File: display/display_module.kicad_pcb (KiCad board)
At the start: 2 copper layers, 38.5 x 20 mm, 14 parts, among them J1 DISPLAY FPC, J2 FPC LOGIC, J4 DF40

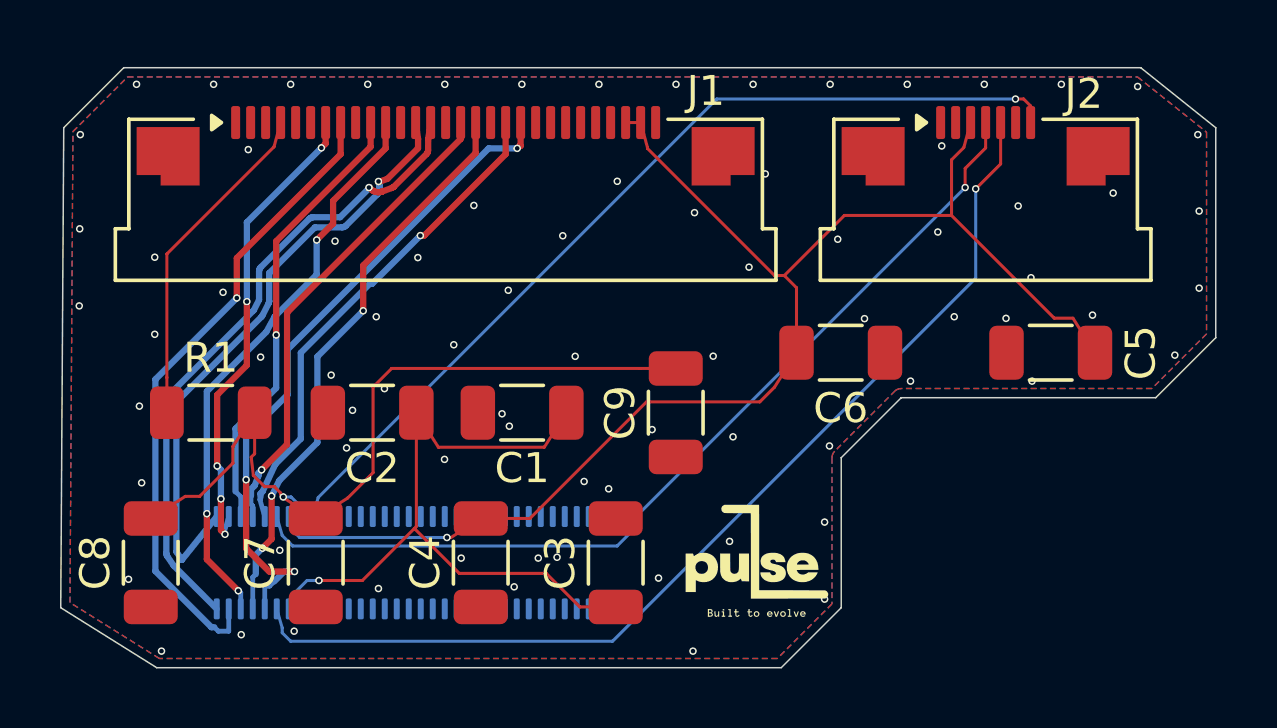
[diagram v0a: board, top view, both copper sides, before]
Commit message: fix the interrupted gnd plane by moving to 4 layers and adding gnd zones.
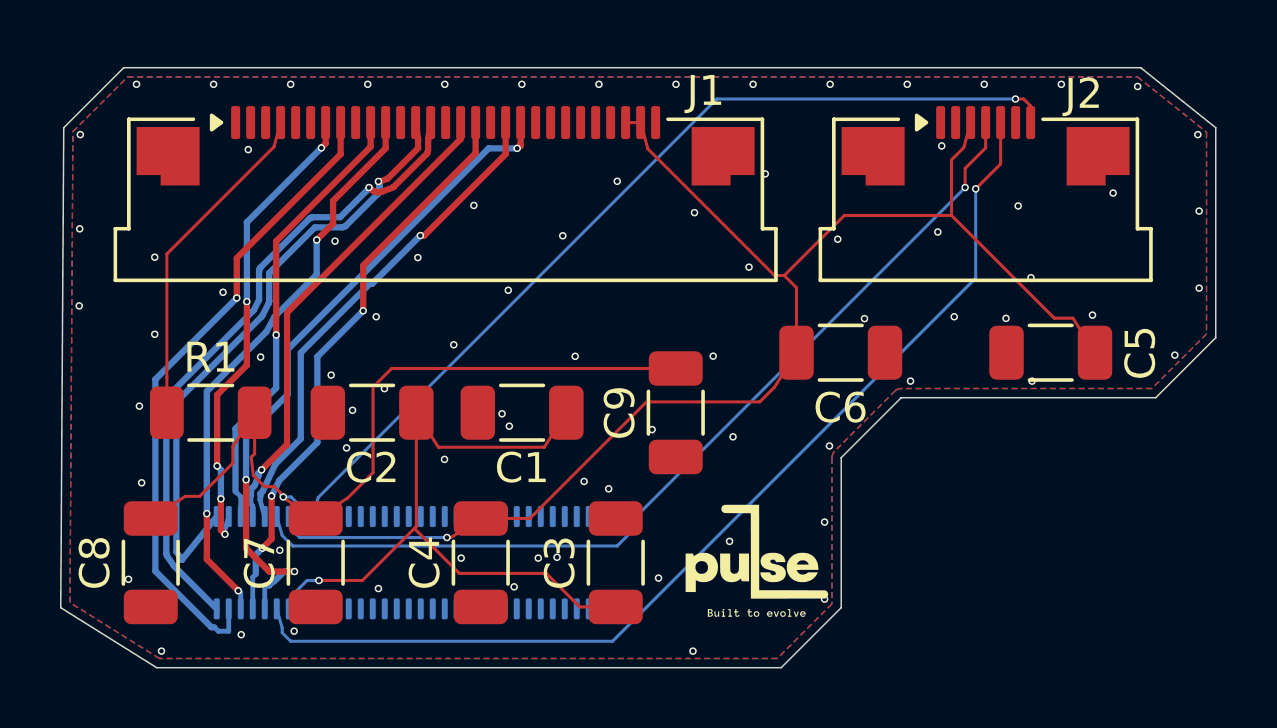
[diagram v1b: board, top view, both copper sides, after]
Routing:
- added copper zone on In1.Cu, net GND
- added copper zone on In2.Cu, net GND
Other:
- copper layers 2 -> 4

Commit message: concetrate center of mass ontop of display DF40c
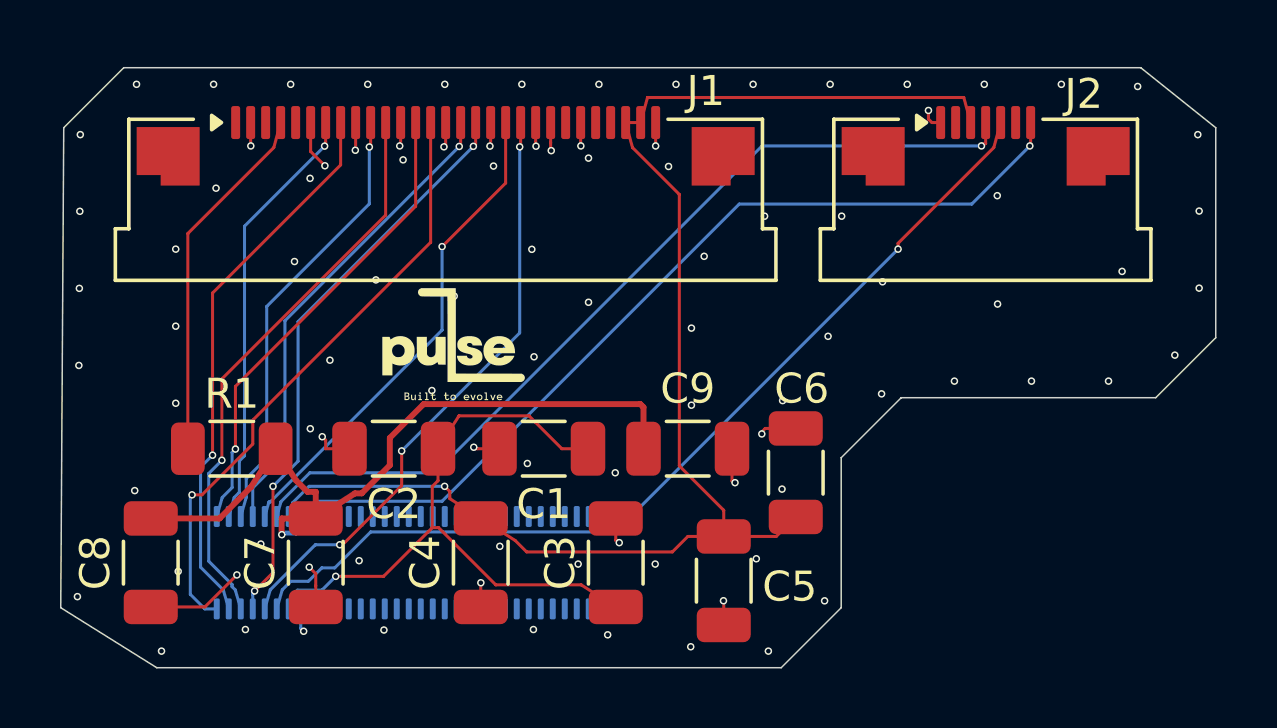
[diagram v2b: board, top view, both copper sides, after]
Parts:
- moved C5 13.3 mm to (139.6, 81.6), turned to 90 degrees
- moved G*** 12.4 mm to (130.6, 73.8)
- moved C6 4.27 mm to (142.0, 78.0), turned to -90 degrees
- moved C2 1.40 mm to (128.6, 77.2)
- moved C1 1.40 mm to (133.6, 77.2)
- moved R1 1.39 mm to (123.2, 77.2)
- moved C9 1.26 mm to (138.4, 77.2), turned to 180 degrees
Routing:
- net GND: track 0.00 -> 22.4 mm, vias 80 -> 96
- net DSI-CLK-N: track 20.5 -> 15.8 mm
- net DSI-0-P: track 21.5 -> 18.5 mm
- net I2C3-SDA: track 34.6 -> 31.8 mm
- net DSI-3-P: track 22.4 -> 20.2 mm
- net DSI-0-N: track 16.0 -> 14.4 mm, vias 5 -> 1
- net I2C3-SCL: track 31.2 -> 29.7 mm
- net +5V: track 23.4 -> 22.0 mm
- net +3.7VBAT: track 26.7 -> 25.4 mm
- net DSI-CLK-P: track 21.6 -> 20.3 mm
- net Net-(J1-Pin_4): track 11.2 -> 12.1 mm
- net RST: track 30.6 -> 30.0 mm
- net DSI-1-P: track 19.1 -> 19.0 mm, vias 3 -> 1
- removed copper zone on B.Cu, net GND
- removed copper zone on F.Cu, net GND

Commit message: final review change (board was ordered, prod ready verSion)
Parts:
- J1: value DISPLAY FPC -> THD THD0515-29CL-SN; footprint Connector_FFC-FPC:Amphenol_F32R-1A7x1-11029_1x29-1MP_P0.5mm_Horizontal -> Connector_FFC-FPC:FPC-29-P0.5
- J2: footprint Connector_FFC-FPC:Amphenol_F32Q-1A7x1-11007_1x07-1MP_P0.5mm_Horizontal -> Connector_FFC-FPC:FPC_7
- J4: footprint Connector_Hirose_DF40:Hirose_DF40C(2.0)-70DS-0.4V_2x35_P0.4mm -> Connector_Hirose_DF40:Hirose_DF40C-34DS-0.4V_2x17_P0.4mm
- moved J1 1.12 mm to (130.7, 70.3), turned to 180 degrees
- moved J2 1.10 mm to (148.2, 70.3), turned to 180 degrees
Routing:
- net Net-(J1-Pin_4): track 12.1 -> 21.7 mm
- net RST: track 30.0 -> 22.8 mm, vias 1 -> 3
- net DSI-3-N: track 16.4 -> 9.63 mm
- net I2C3-SDA: track 31.8 -> 25.9 mm
- net DSI-2-N: track 16.0 -> 10.5 mm
- net DSI-CLK-P: track 20.3 -> 15.0 mm
- net I2C3-SCL: track 29.7 -> 25.3 mm
- net GND: track 22.4 -> 18.3 mm, vias 96 -> 87
- net +3.3V: track 46.7 -> 42.7 mm, vias 1 -> 2
- net DSI-1-P: track 19.0 -> 16.5 mm
- net DSI-3-P: track 20.2 -> 18.2 mm, vias 3 -> 1
- net +3.7VBAT: track 25.4 -> 23.6 mm
- net DSI-0-N: track 14.4 -> 12.8 mm
- net DSI-2-P: track 19.3 -> 17.8 mm, vias 3 -> 1
- net DSI-CLK-N: track 15.8 -> 14.6 mm, vias 1 -> 3
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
